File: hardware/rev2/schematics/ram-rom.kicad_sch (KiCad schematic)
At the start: 7 parts, among them U10 28C256, U11 28C256, U12 MT16D832

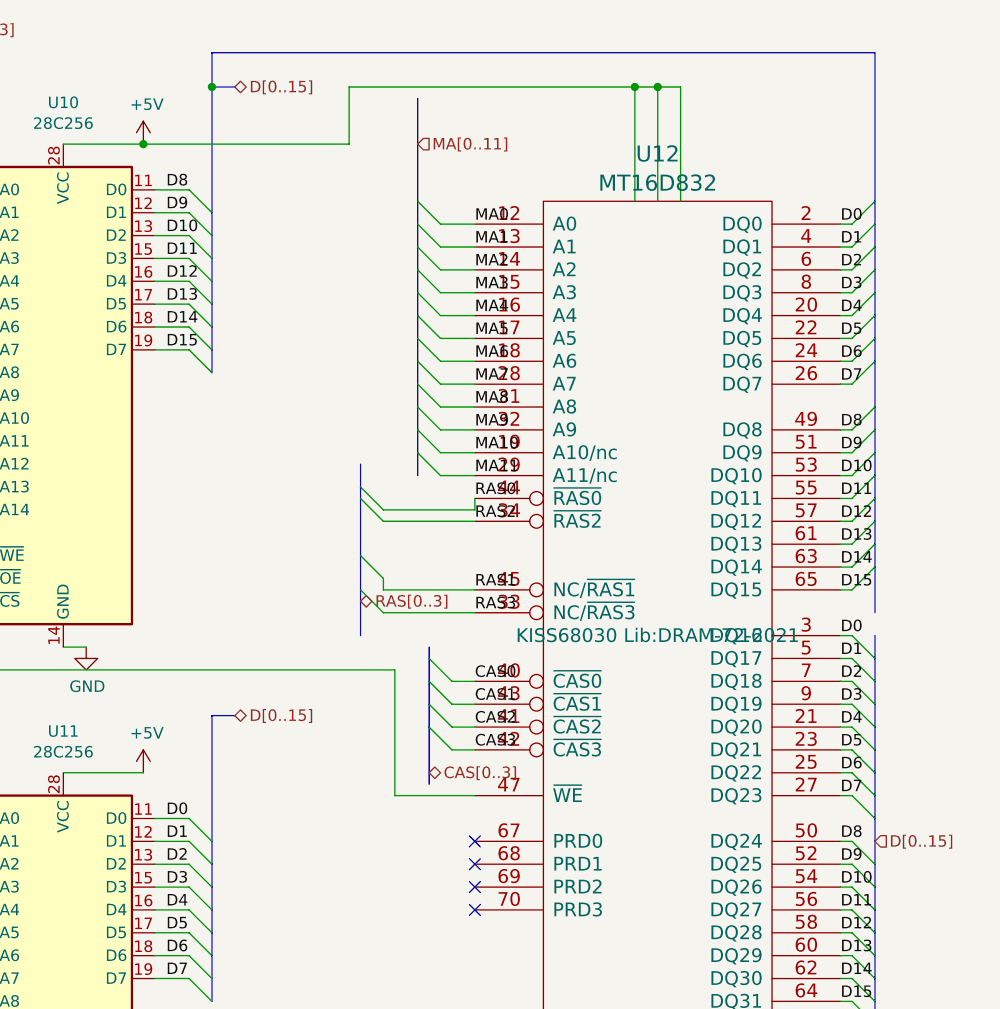
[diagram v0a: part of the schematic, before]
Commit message: ERC fixes, part 1
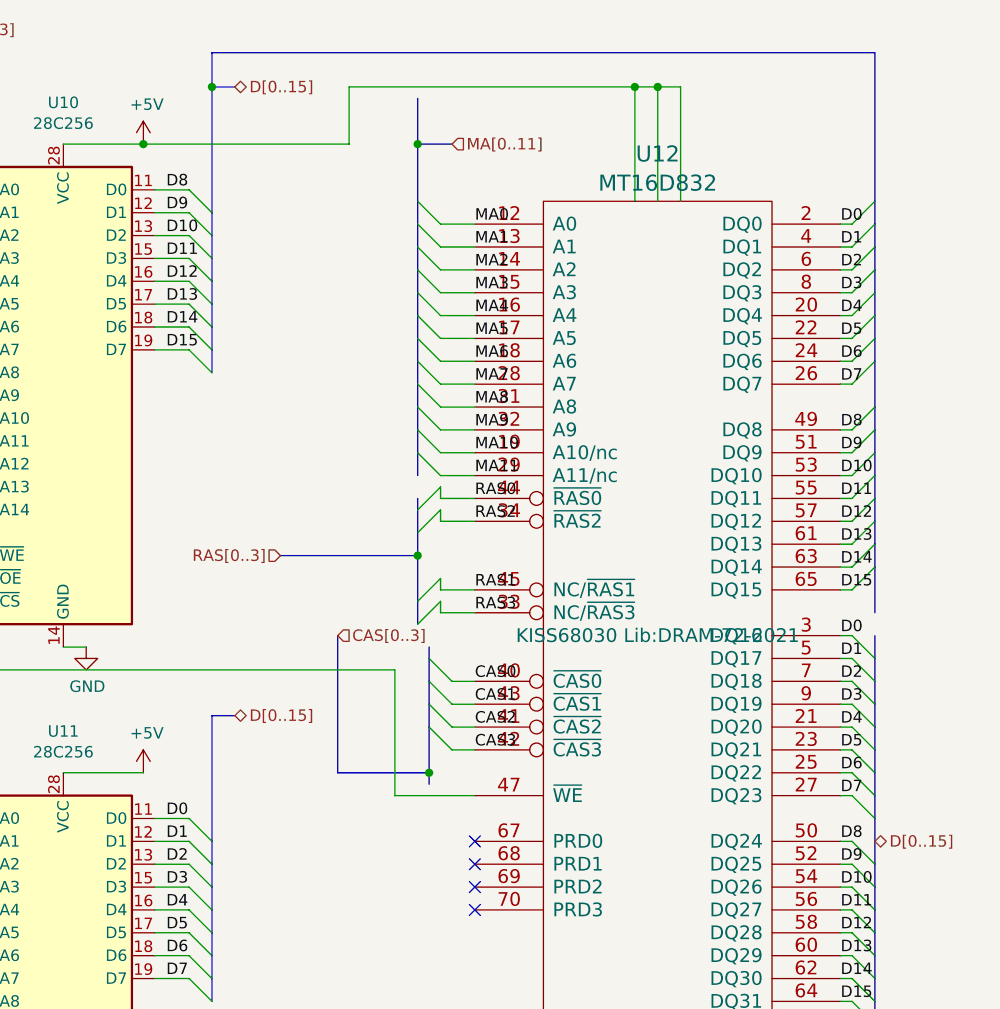
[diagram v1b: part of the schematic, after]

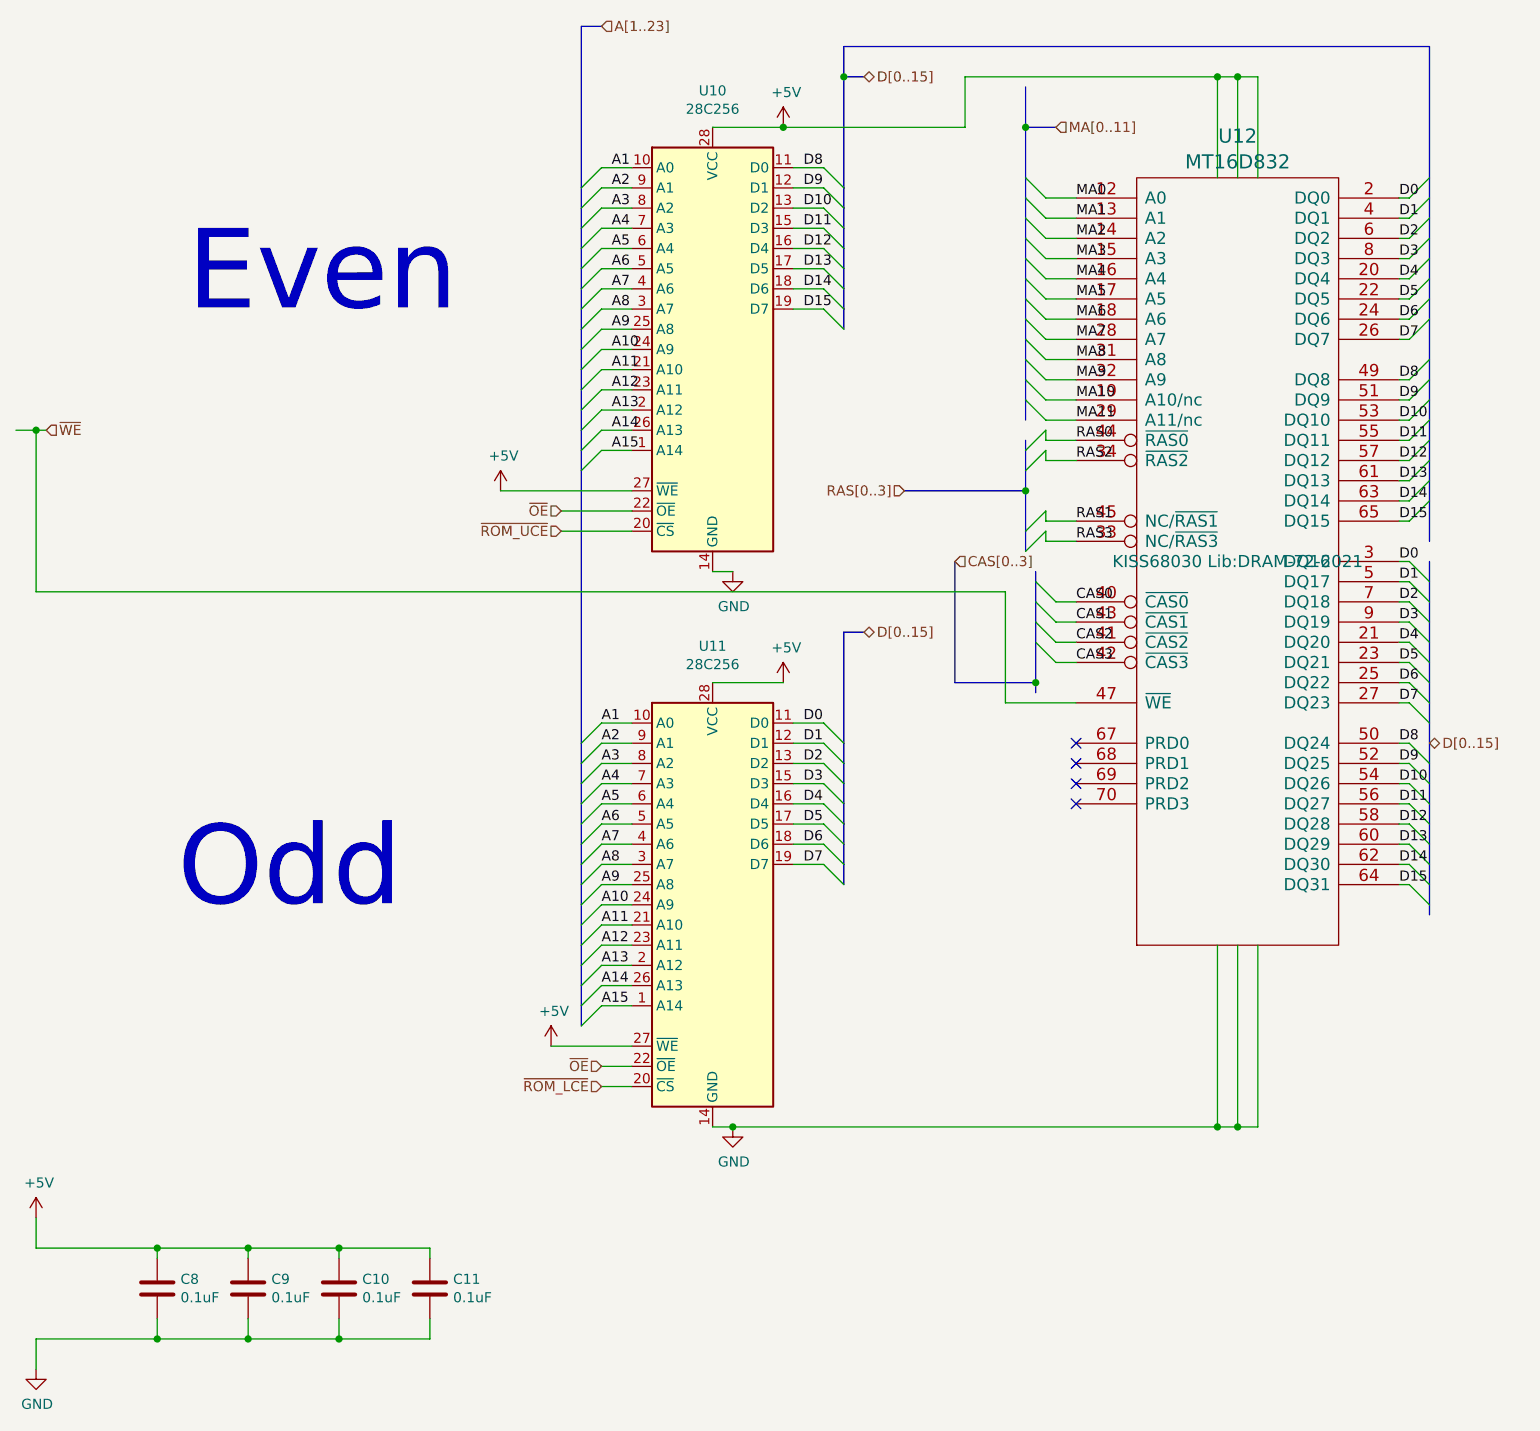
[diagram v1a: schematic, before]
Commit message: ERC fixes part 2. No more errors reported. Re-routed the PCB.
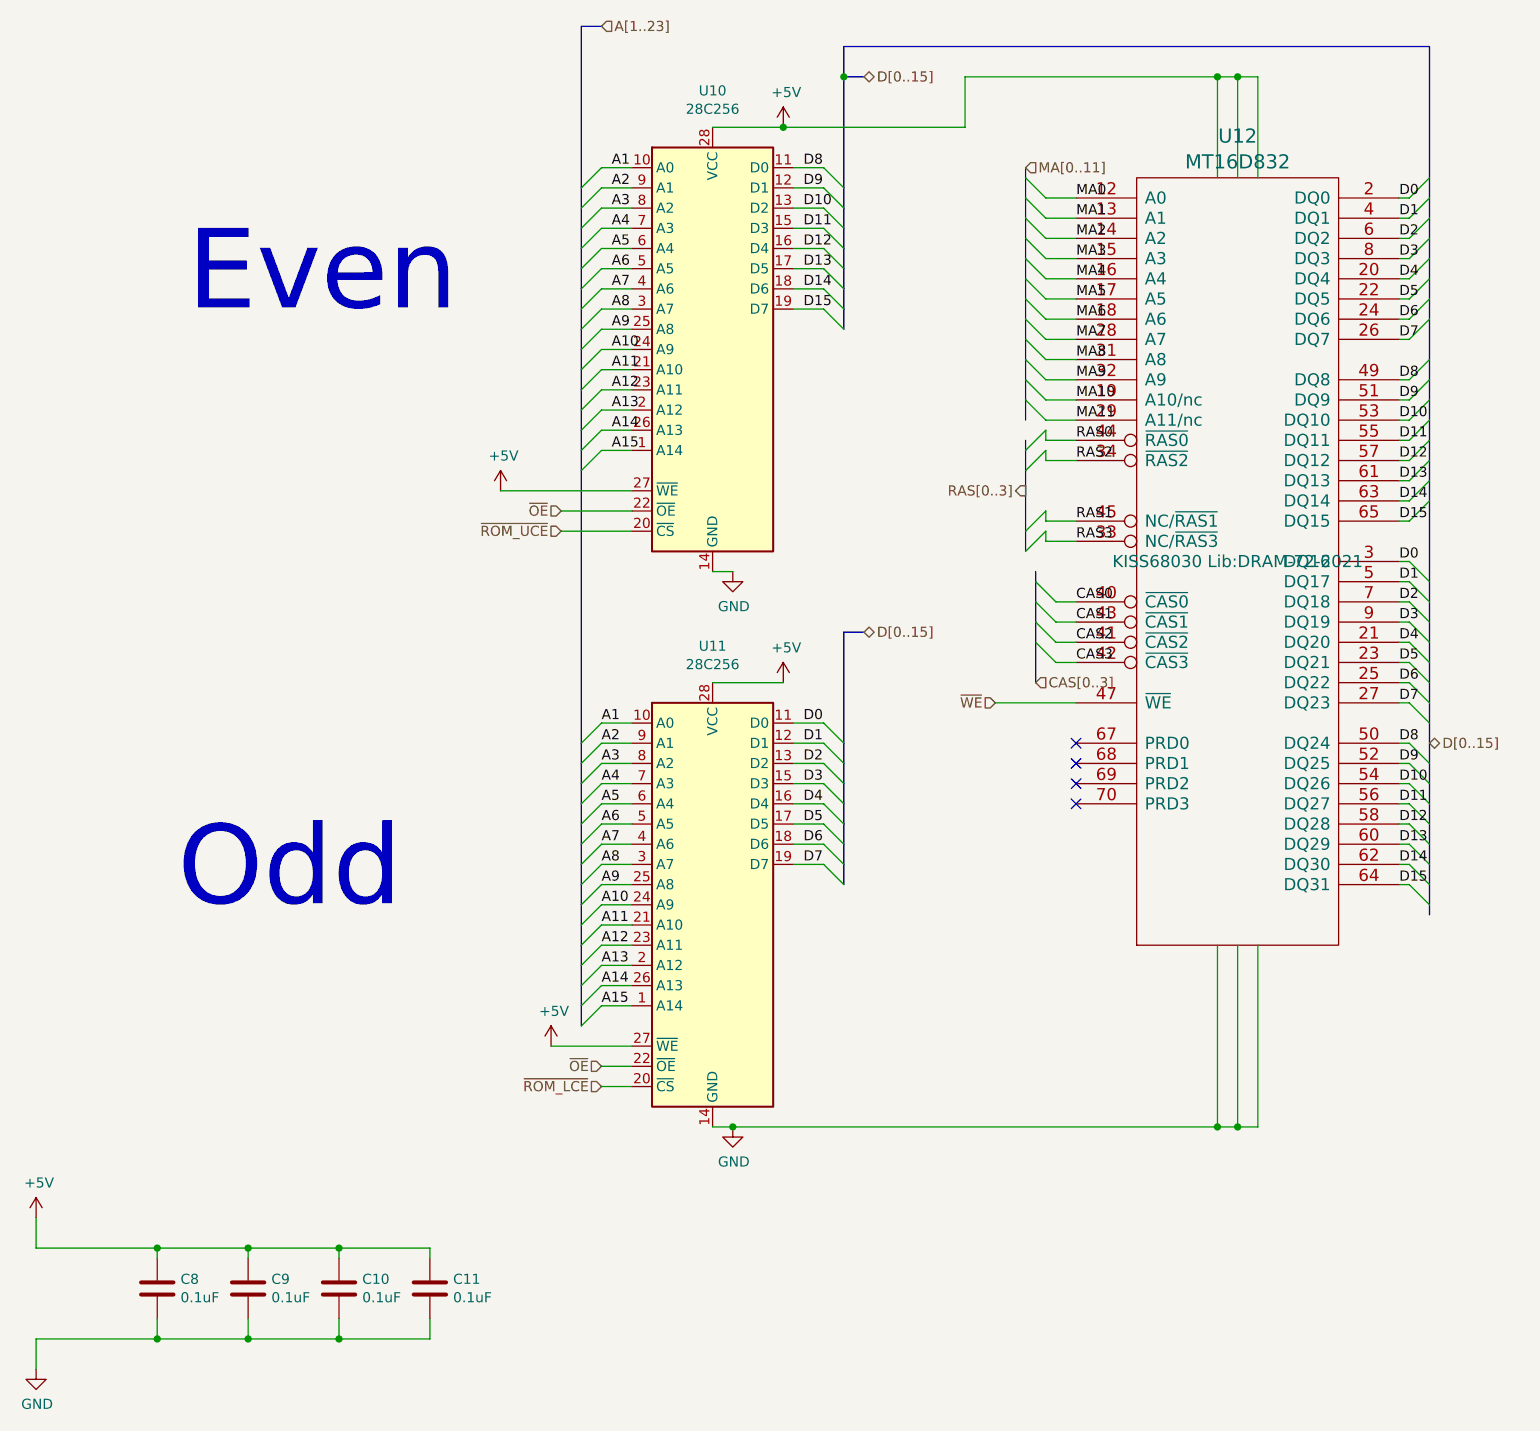
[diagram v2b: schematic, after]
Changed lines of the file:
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@@
 	)
 	(junction
-		(at 78.74 71.12)
-		(diameter 0)
-		(color 0 0 0 0)
-	)
-	(junction
 		(at 180.34 26.67)
 		(diameter 0)
@@
 	)
 	(junction
-		(at 203.2 33.02)
-		(diameter 0)
-		(color 0 0 0 0)
-	)
-	(junction
 		(at 227.33 158.75)
 		(diameter 0)
@@
 	)
 	(junction
-		(at 204.47 102.87)
-		(diameter 0)
-		(color 0 0 0 0)
-	)
-	(junction
 		(at 227.33 26.67)
 		(diameter 0)
@@
 		(color 0 0 0 0)
 	)
-	(junction
-		(at 203.2 78.74)
-		(diameter 0)
-		(color 0 0 0 0)
-	)
 	(no_connect
 		(at 209.55 118.11)
@@
 		)
 	)
-	(wire
-		(pts
-			(xy 200.66 91.44) (xy 78.74 91.44)
-		)
-		(stroke
-			(width 0)
-			(type default)
-		)
-	)
 	(bus
 		(pts
@@
 		)
 	)
-	(bus
-		(pts
-			(xy 194.31 102.87) (xy 204.47 102.87)
-		)
-		(stroke
-			(width 0)
-			(type default)
-		)
-	)
 	(wire
 		(pts
@@
 	(wire
 		(pts
-			(xy 78.74 91.44) (xy 78.74 71.12)
-		)
-		(stroke
-			(width 0)
-			(type default)
-		)
-	)
-	(wire
-		(pts
 			(xy 153.67 138.43) (xy 149.86 138.43)
 		)
@@
 	(bus
 		(pts
-			(xy 204.47 102.87) (xy 204.47 104.14)
-		)
-		(stroke
-			(width 0)
-			(type default)
-		)
-	)
-	(bus
-		(pts
 			(xy 180.34 123.19) (xy 180.34 125.73)
 		)
@@
 	(bus
 		(pts
-			(xy 203.2 78.74) (xy 203.2 83.82)
+			(xy 203.2 76.2) (xy 203.2 83.82)
 		)
 		(stroke
@@
 	(wire
 		(pts
-			(xy 209.55 105.41) (xy 200.66 105.41)
+			(xy 199.39 105.41) (xy 209.55 105.41)
 		)
 		(stroke
@@
 	(bus
 		(pts
-			(xy 187.96 78.74) (xy 203.2 78.74)
-		)
-		(stroke
-			(width 0)
-			(type default)
-		)
-	)
-	(bus
-		(pts
 			(xy 147.32 128.27) (xy 147.32 130.81)
 		)
@@
 	(bus
 		(pts
-			(xy 203.2 76.2) (xy 203.2 78.74)
-		)
-		(stroke
-			(width 0)
-			(type default)
-		)
-	)
-	(bus
-		(pts
 			(xy 147.32 20.32) (xy 147.32 40.64)
 		)
@@
 		)
 	)
-	(wire
-		(pts
-			(xy 200.66 105.41) (xy 200.66 91.44)
-		)
-		(stroke
-			(width 0)
-			(type default)
-		)
-	)
 	(bus
 		(pts
@@
 	(bus
 		(pts
-			(xy 254 87.63) (xy 254 90.17)
+			(xy 254 80.01) (xy 254 90.17)
 		)
 		(stroke
@@
 		)
 	)
-	(bus
-		(pts
-			(xy 207.01 33.02) (xy 203.2 33.02)
-		)
-		(stroke
-			(width 0)
-			(type default)
-		)
-	)
 	(wire
 		(pts
@@
 	(wire
 		(pts
-			(xy 76.2 71.12) (xy 78.74 71.12)
-		)
-		(stroke
-			(width 0)
-			(type default)
-		)
-	)
-	(wire
-		(pts
 			(xy 116.84 185.42) (xy 128.27 185.42)
 		)
@@
 	(bus
 		(pts
-			(xy 203.2 33.02) (xy 203.2 39.37)
+			(xy 203.2 38.1) (xy 203.2 39.37)
 		)
 		(stroke
@@
 	(wire
 		(pts
-			(xy 78.74 71.12) (xy 80.01 71.12)
-		)
-		(stroke
-			(width 0)
-			(type default)
-		)
-	)
-	(wire
-		(pts
 			(xy 163.83 158.75) (xy 166.37 158.75)
 		)
@@
 	(bus
 		(pts
-			(xy 203.2 27.94) (xy 203.2 33.02)
-		)
-		(stroke
-			(width 0)
-			(type default)
-		)
-	)
-	(bus
-		(pts
 			(xy 147.32 133.35) (xy 147.32 135.89)
 		)
@@
 		)
 	)
-	(bus
-		(pts
-			(xy 254 80.01) (xy 254 85.09)
-		)
-		(stroke
-			(width 0)
-			(type default)
-		)
-	)
 	(wire
 		(pts
@@
 	(bus
 		(pts
-			(xy 194.31 87.63) (xy 194.31 102.87)
-		)
-		(stroke
-			(width 0)
-			(type default)
-		)
-	)
-	(bus
-		(pts
 			(xy 147.32 76.2) (xy 147.32 110.49)
 		)
@@
 	(label "RAS2"
 		(at 209.55 74.93 0)
+		(fields_autoplaced yes)
 		(effects
 			(font
@@
 	(label "RAS0"
 		(at 209.55 72.39 0)
+		(fields_autoplaced yes)
 		(effects
 			(font
@@
 	(label "RAS1"
 		(at 209.55 82.55 0)
+		(fields_autoplaced yes)
 		(effects
 			(font
@@
 	(label "RAS3"
 		(at 209.55 85.09 0)
+		(fields_autoplaced yes)
 		(effects
 			(font
@@
 	(hierarchical_label "CAS[0..3]"
 		(shape input)
-		(at 194.31 87.63 0)
+		(at 204.47 102.87 0)
 		(fields_autoplaced yes)
 		(effects
@@
 	(hierarchical_label "MA[0..11]"
 		(shape input)
-		(at 207.01 33.02 0)
+		(at 203.2 38.1 0)
 		(fields_autoplaced yes)
 		(effects
@@
 	)
 	(hierarchical_label "RAS[0..3]"
-		(shape input)
-		(at 187.96 78.74 180)
+		(shape output)
+		(at 203.2 78.74 180)
 		(fields_autoplaced yes)
 		(effects
@@
 	(hierarchical_label "~{WE}"
 		(shape input)
-		(at 80.01 71.12 0)
+		(at 199.39 105.41 180)
 		(fields_autoplaced yes)
 		(effects
@@
 				(size 1.27 1.27)
 			)
-			(justify left)
+			(justify right)
 		)
 	)
